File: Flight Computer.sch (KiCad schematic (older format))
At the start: 17 parts, among them J1 BB_6.35mm, J2 Sig_Out, U1 BMP280, U2 Teensy3.5, U3 Adafruit_GPS_THT

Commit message: New V2 integrated flight computer schematic Moved MCU to its own sheet Added datasheets Added KiCAD footprint submodule
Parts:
- removed J2: Sig_Out, Pin_Headers:Pin_Header_Straight_1x02_Pitch2.54mm, symbol Connector_Generic:Conn_01x02
- removed U2: Teensy3.5, Flight-Computer:Teensy35_36, symbol Teensy:Teensy3.5
- added D1, D10, D11, D12, D13, D14, D15, D16, D2, D3, D4, D5, D6, D7, D8, D9: BAT54S, Package_TO_SOT_SMD:SOT-23, symbol Diode:BAT54S
- gave numbers to parts that had none: 1
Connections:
- net labels removed: LANDED, LAUNCHED
- wire segments 92 -> 86
- no-connect marks 86 -> 24

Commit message: Updated pinmap
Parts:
- removed D1, D10, D11, D12, D13, D14, D15, D16, D2, D3, D4, D5, D6, D7, D8, D9: BAT54S, Package_TO_SOT_SMD:SOT-23, symbol Diode:BAT54S
- removed J1: BB_6.35mm, TerminalBlock:TerminalBlock_bornier-6_P5.08mm, symbol Connector:Screw_Terminal_01x06
- added R?: 10k, Resistor_THT:R_Axial_DIN0207_L6.3mm_D2.5mm_P10.16mm_Horizontal, symbol Device:R
- added R?: 33k, Resistor_THT:R_Axial_DIN0207_L6.3mm_D2.5mm_P10.16mm_Horizontal, symbol Device:R
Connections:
- net labels added: ACT, ADC, ADC1, ADC2, I2C1, SPI1, SPI2, USART1_2, USART1_RX, USART1_TX, USART2_RX, USART2_TX
- net labels removed: BAT_V_DIV, GPS_RX, GPS_TX, XBEE_CTS, XBEE_RTS, XBEE_RX, XBEE_TX
- wire segments 86 -> 76
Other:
- moved on the sheet: C4, C5, R6, R7, U3, XB1

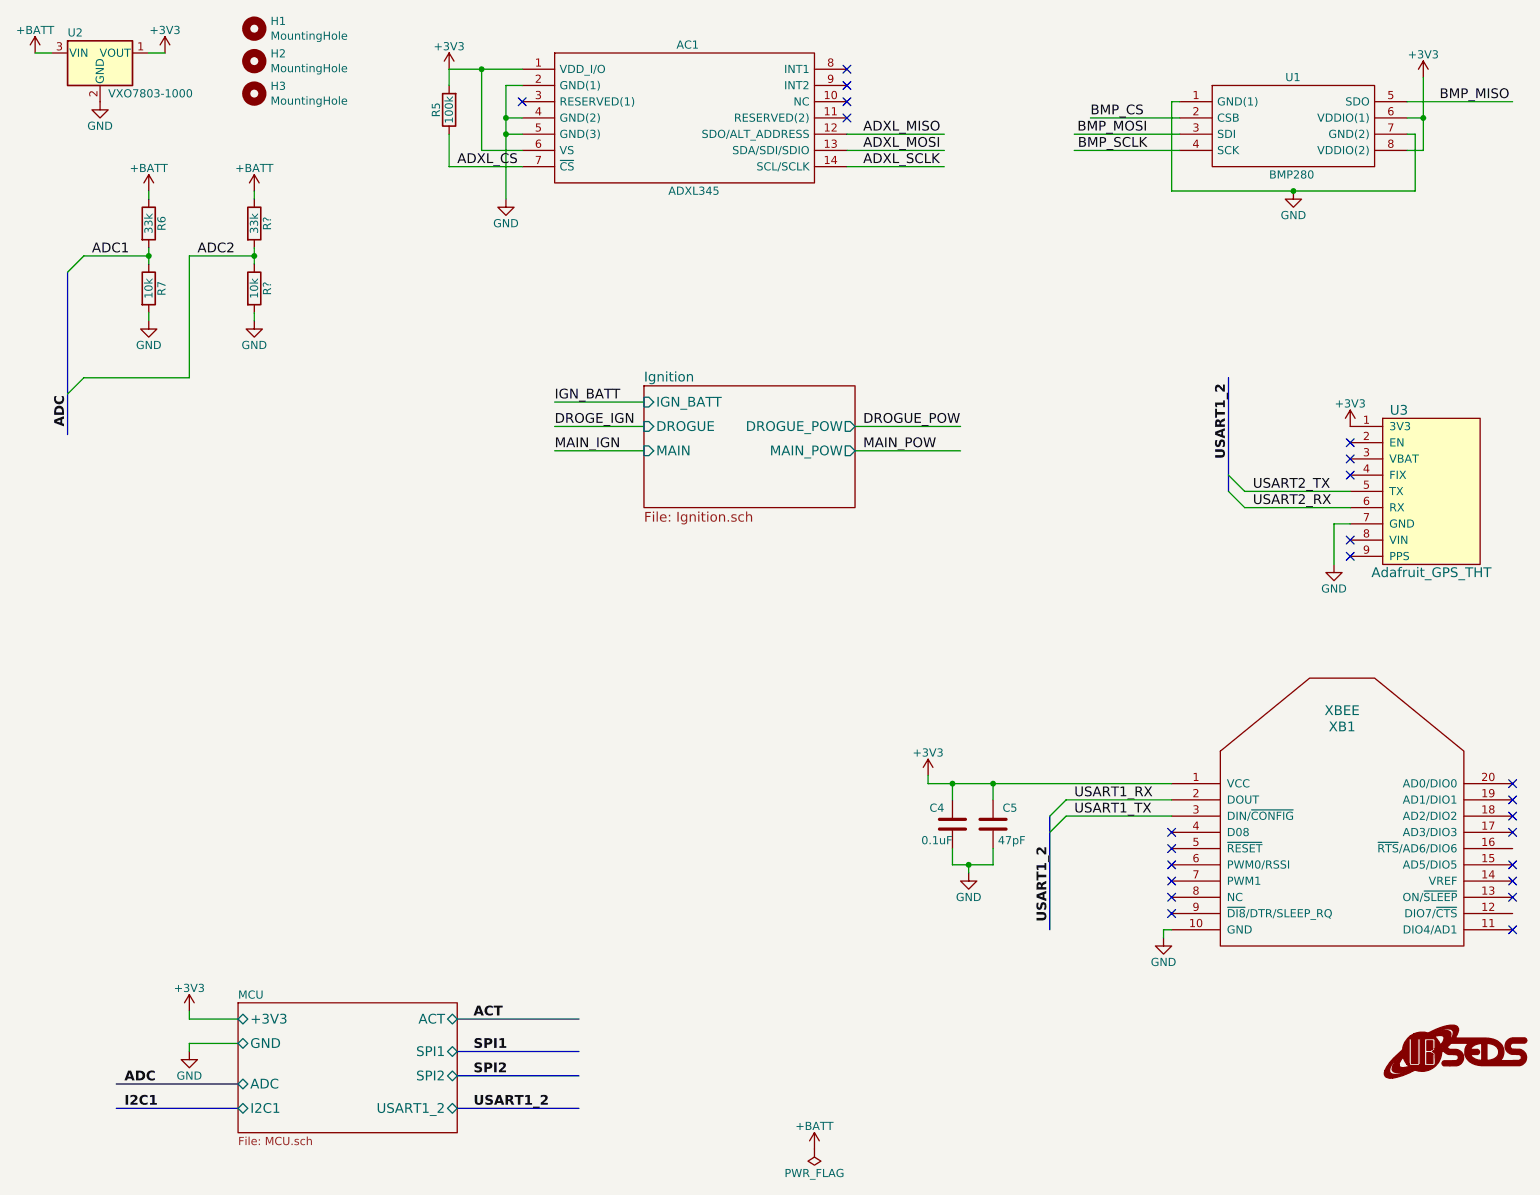
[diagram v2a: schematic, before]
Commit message: New pyro transistors New IO connector Changed SPI pins
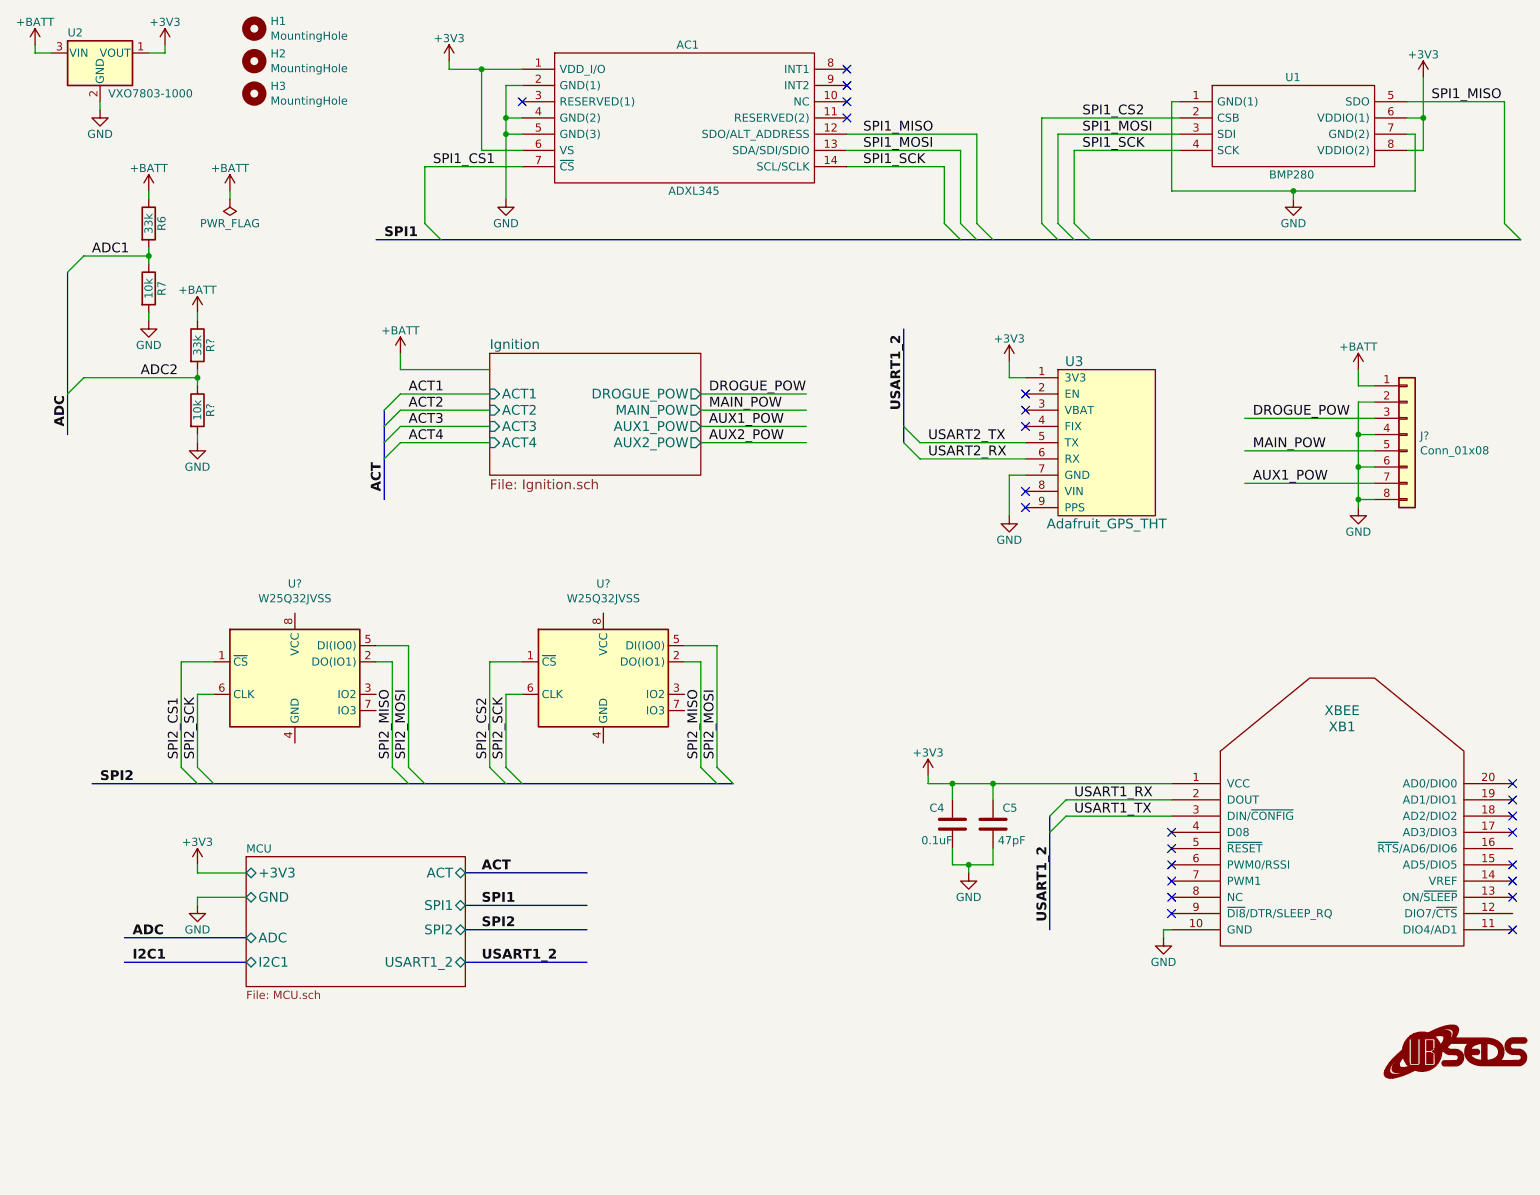
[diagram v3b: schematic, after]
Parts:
- removed R5: 100k, Resistor_THT:R_Axial_DIN0207_L6.3mm_D2.5mm_P10.16mm_Horizontal, symbol Device:R
- added J?: Conn_01x08, symbol Connector_Generic:Conn_01x08
- added U? (x2): W25Q32JVSS, Package_SO:SOIC-8_5.23x5.23mm_P1.27mm, symbol Memory_Flash:W25Q32JVSS
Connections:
- net labels added: ACT1, ACT2, ACT3, ACT4, AUX1_POW, AUX2_POW, SPI1_CS1, SPI1_CS2, SPI1_MISO, SPI1_MOSI, SPI1_SCK, SPI2_CS1, SPI2_CS2, SPI2_MISO, SPI2_MOSI, SPI2_SCK
- net labels removed: ADXL_CS, ADXL_MISO, ADXL_MOSI, ADXL_SCLK, BMP_CS, BMP_MISO, BMP_MOSI, BMP_SCLK, DROGE_IGN, IGN_BATT, MAIN_IGN
- wire segments 76 -> 126
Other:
- moved on the sheet: R?, U3

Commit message: Starting to fix ERC errors
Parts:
- J1: renamed from J?; footprint (none) -> Connector_PinHeader_2.54mm:PinHeader_1x08_P2.54mm_Vertical
- R1: renamed from R6; footprint Resistor_THT:R_Axial_DIN0207_L6.3mm_D2.5mm_P10.16mm_Horizontal -> Resistor_SMD:R_1206_3216Metric_Pad1.42x1.75mm_HandSolder
- R2: renamed from R7; footprint Resistor_THT:R_Axial_DIN0207_L6.3mm_D2.5mm_P10.16mm_Horizontal -> Resistor_SMD:R_1206_3216Metric_Pad1.42x1.75mm_HandSolder
- R3, R4: renamed from R?; footprint Resistor_THT:R_Axial_DIN0207_L6.3mm_D2.5mm_P10.16mm_Horizontal -> Resistor_SMD:R_1206_3216Metric_Pad1.42x1.75mm_HandSolder
- gave numbers to parts that had none: 2
- renumbered C4 to C1, C5 to C2, U2 to U1, U3 to U4, U1 to U5

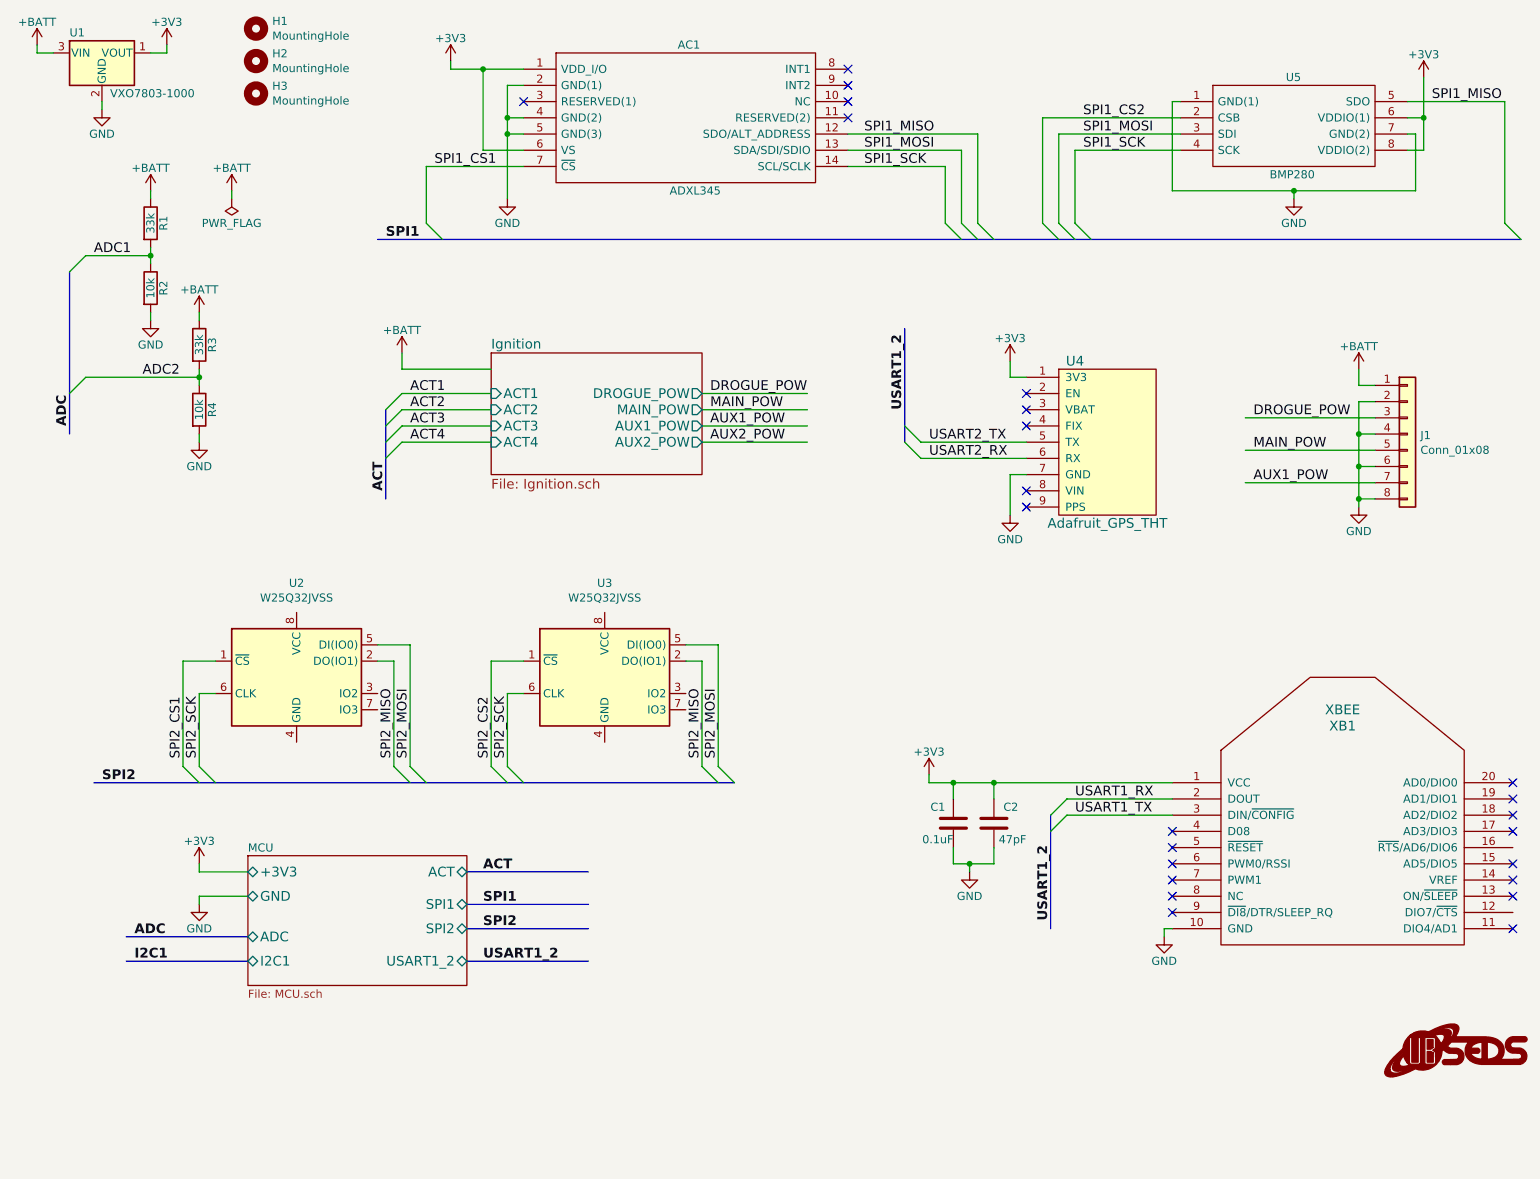
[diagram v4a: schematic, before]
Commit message: Fixed most ERC errors
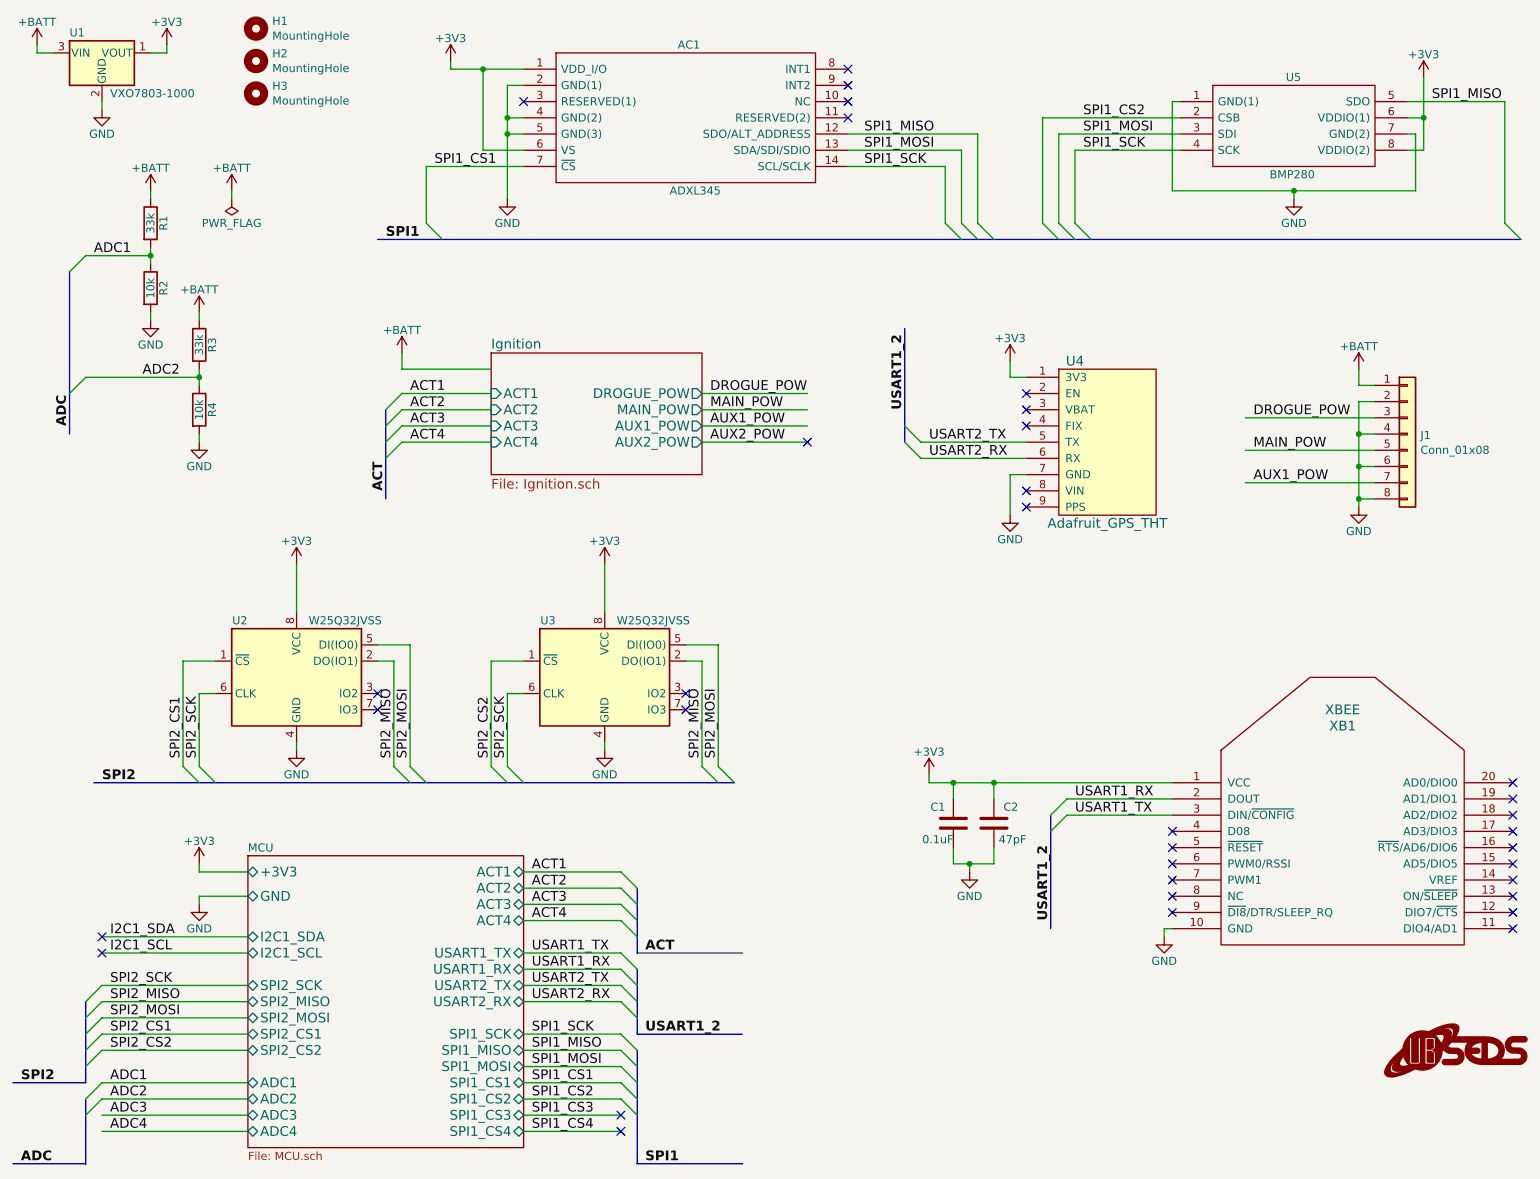
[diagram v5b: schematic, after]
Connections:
- net labels added: ADC3, ADC4, I2C1_SCL, I2C1_SDA, SPI1_CS3, SPI1_CS4
- net labels removed: I2C1
- wire segments 126 -> 148
- no-connect marks 24 -> 35
